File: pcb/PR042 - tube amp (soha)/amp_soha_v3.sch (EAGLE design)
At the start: 55 parts, among them IC1 NE5532, IC2 7812, IC3 7912, Q1 J113, Q2 J113, Q3 J113, Q4 J113

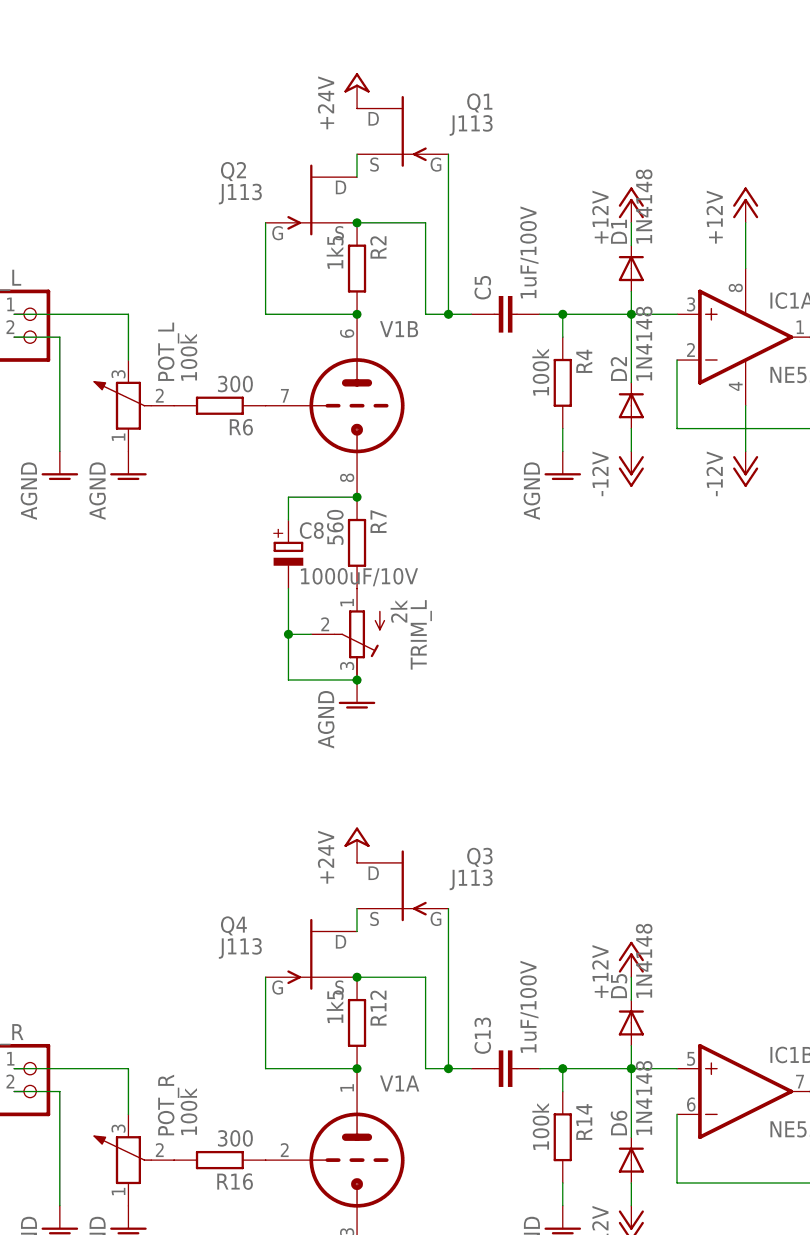
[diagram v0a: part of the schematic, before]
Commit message: 
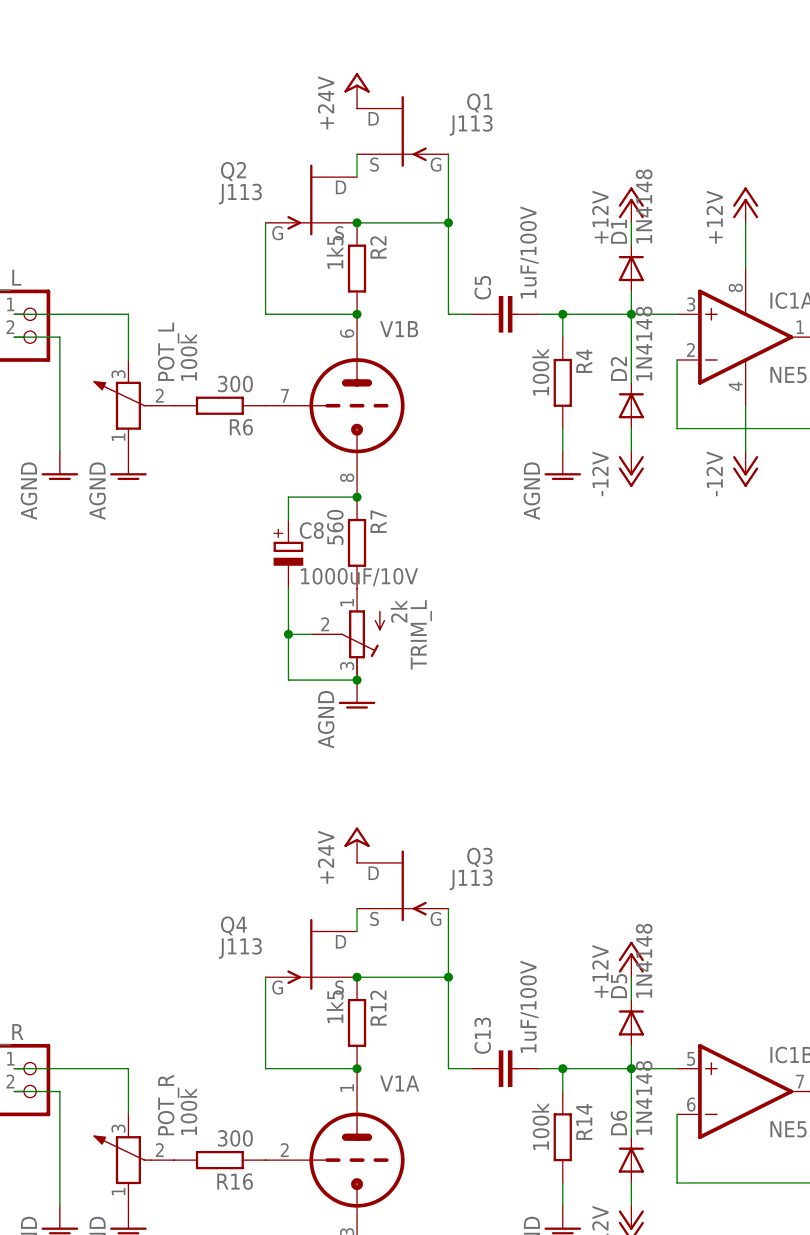
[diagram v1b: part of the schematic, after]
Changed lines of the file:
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@@
 <?xml version="1.0" encoding="utf-8"?>
 <!DOCTYPE eagle SYSTEM "eagle.dtd">
-<eagle version="6.5.0">
+<eagle version="6.4">
 <drawing>
 <settings>
@@
 <pinref part="Q2" gate="G$1" pin="S"/>
 <junction x="185.42" y="58.42"/>
-<wire x1="185.42" y1="58.42" x2="193.04" y2="58.42" width="0.1524" layer="91"/>
-<wire x1="193.04" y1="58.42" x2="193.04" y2="48.26" width="0.1524" layer="91"/>
+<wire x1="185.42" y1="58.42" x2="195.58" y2="58.42" width="0.1524" layer="91"/>
 <pinref part="Q1" gate="G$1" pin="G"/>
 <pinref part="C5" gate="G$1" pin="1"/>
+<wire x1="195.58" y1="58.42" x2="195.58" y2="48.26" width="0.1524" layer="91"/>
 <wire x1="195.58" y1="48.26" x2="198.12" y2="48.26" width="0.1524" layer="91"/>
-<wire x1="195.58" y1="48.26" x2="195.58" y2="66.04" width="0.1524" layer="91"/>
-<junction x="195.58" y="48.26"/>
-<wire x1="193.04" y1="48.26" x2="195.58" y2="48.26" width="0.1524" layer="91"/>
+<wire x1="195.58" y1="58.42" x2="195.58" y2="66.04" width="0.1524" layer="91"/>
+<junction x="195.58" y="58.42"/>
 </segment>
 </net>
@@
 <pinref part="Q4" gate="G$1" pin="S"/>
 <junction x="185.42" y="-25.4"/>
-<wire x1="185.42" y1="-25.4" x2="193.04" y2="-25.4" width="0.1524" layer="91"/>
-<wire x1="193.04" y1="-25.4" x2="193.04" y2="-35.56" width="0.1524" layer="91"/>
+<wire x1="185.42" y1="-25.4" x2="195.58" y2="-25.4" width="0.1524" layer="91"/>
 <pinref part="Q3" gate="G$1" pin="G"/>
-<wire x1="195.58" y1="-35.56" x2="195.58" y2="-17.78" width="0.1524" layer="91"/>
+<wire x1="195.58" y1="-25.4" x2="195.58" y2="-17.78" width="0.1524" layer="91"/>
 <pinref part="C13" gate="G$1" pin="1"/>
+<wire x1="195.58" y1="-25.4" x2="195.58" y2="-35.56" width="0.1524" layer="91"/>
 <wire x1="195.58" y1="-35.56" x2="198.12" y2="-35.56" width="0.1524" layer="91"/>
-<junction x="195.58" y="-35.56"/>
-<wire x1="193.04" y1="-35.56" x2="195.58" y2="-35.56" width="0.1524" layer="91"/>
-</segment>
-</net>
+<junction x="195.58" y="-25.4"/>
+</segment>
+</net>
